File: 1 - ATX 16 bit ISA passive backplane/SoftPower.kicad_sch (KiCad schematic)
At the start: 41 parts, among them J19 ATX POWER, SW1 POWER, U1 74HCT14, U2 74HCT74, U3 LM7905

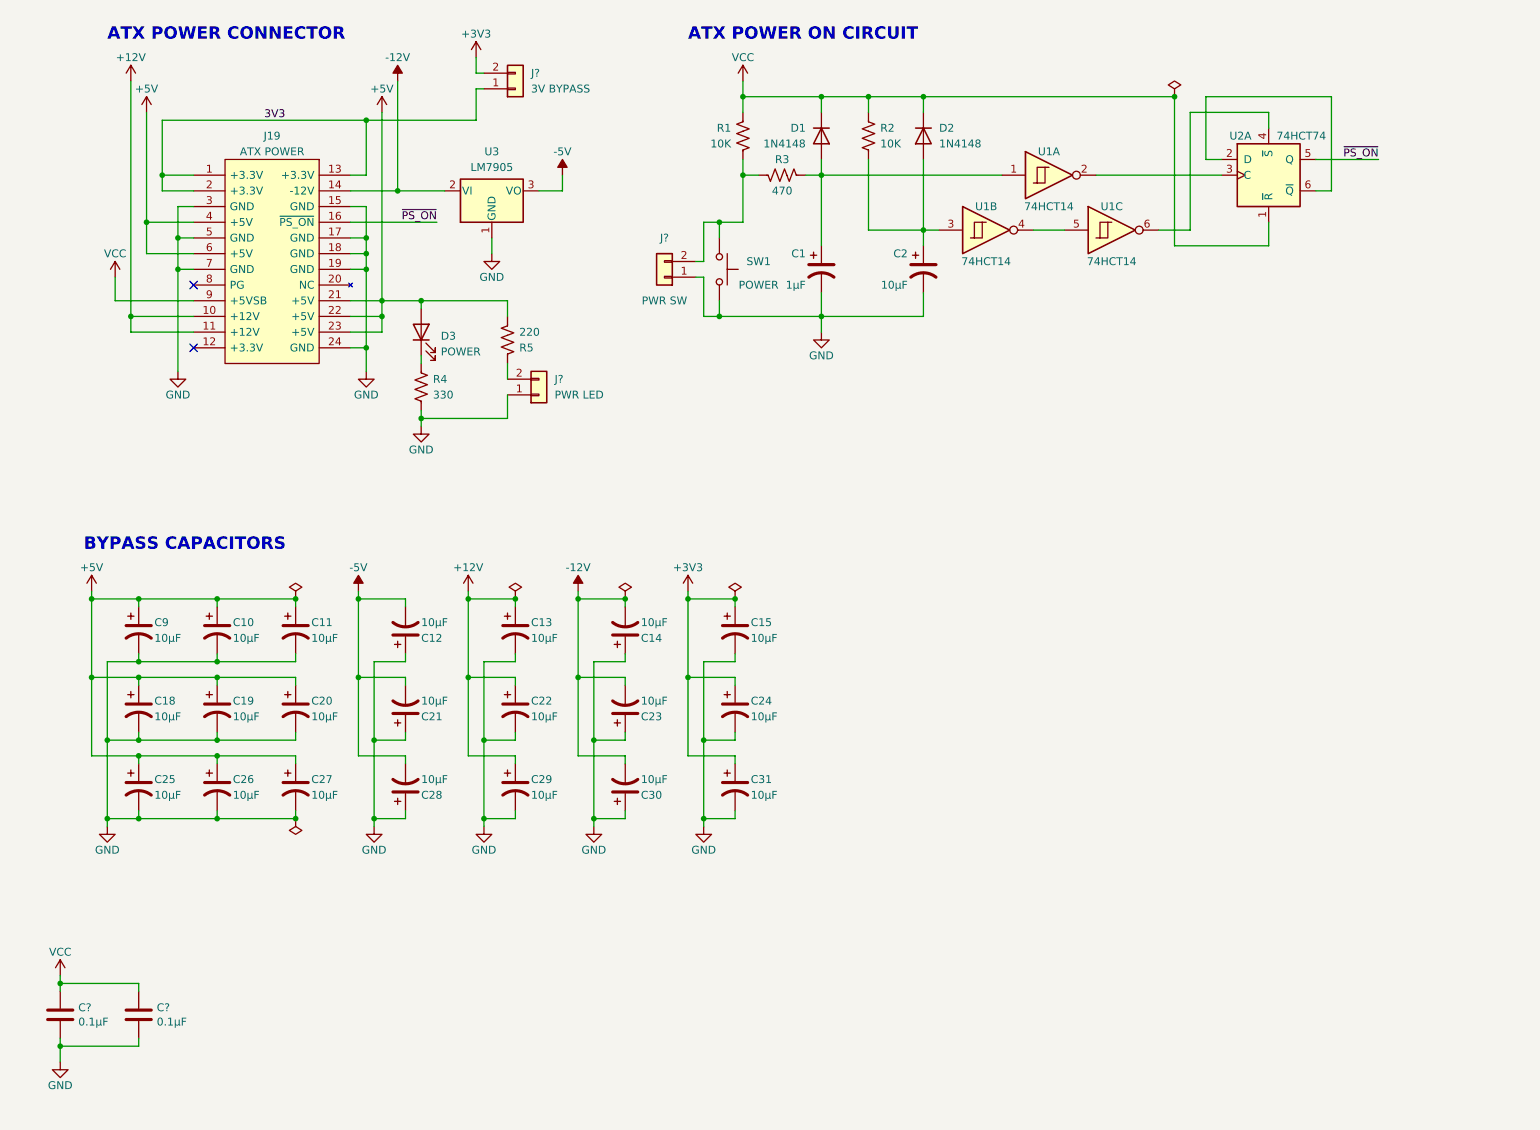
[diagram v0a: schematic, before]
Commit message: Removed unessential components and added capacitors on the bus lanes. Still need work for on the silkscreen side.
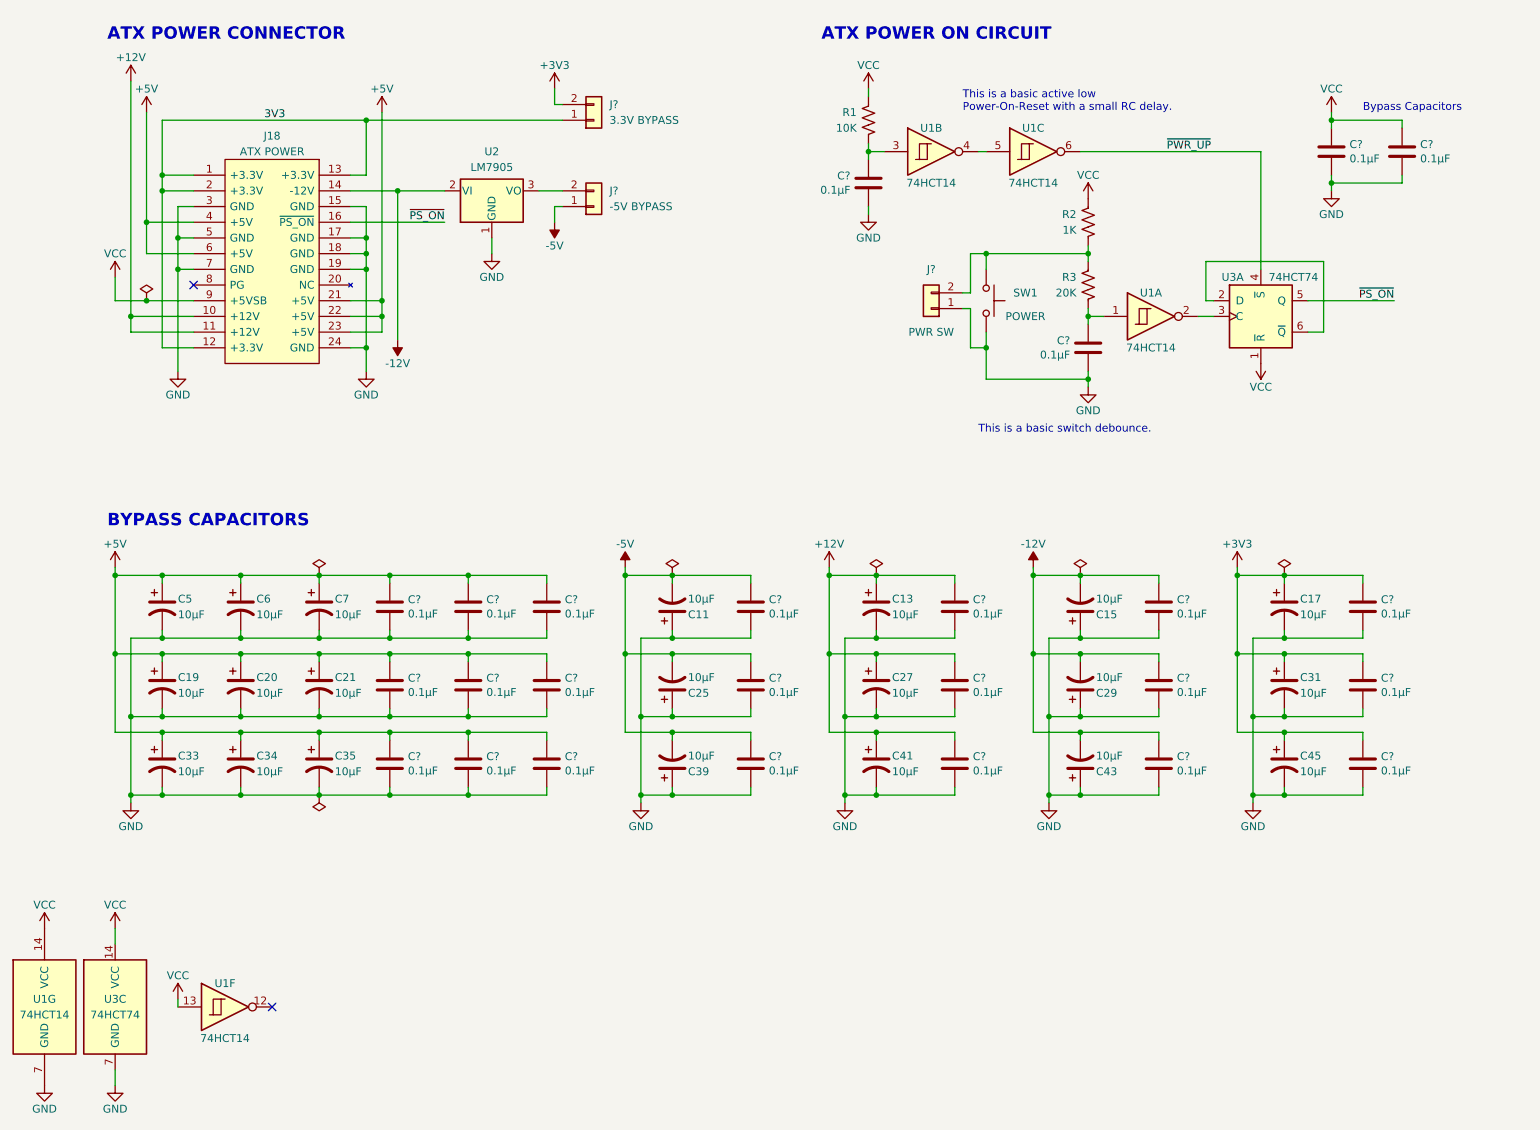
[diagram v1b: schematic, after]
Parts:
- removed C1: 1µF, Capacitor_THT:CP_Radial_D5.0mm_P2.50mm, symbol Device:C_Polarized_US
- removed C2: 10µF, Capacitor_THT:CP_Radial_D6.3mm_P2.50mm, symbol Device:C_Polarized_US
- removed C? (x2): 0.1µF, Capacitor_THT:C_Disc_D3.0mm_W1.6mm_P2.50mm, symbol Device:C
- removed D1, D2: 1N4148, Diode_THT:D_DO-35_SOD27_P7.62mm_Horizontal, symbol Diode:1N4148
- removed D3: POWER, LED_THT:LED_D3.0mm, symbol Device:LED
- removed J?: PWR LED, Connector_PinHeader_2.54mm:PinHeader_1x02_P2.54mm_Vertical, symbol Connector_Generic:Conn_01x02
- removed R4: 330, Resistor_THT:R_Axial_DIN0207_L6.3mm_D2.5mm_P10.16mm_Horizontal, symbol Device:R_US
- removed R5: 220, Resistor_THT:R_Axial_DIN0207_L6.3mm_D2.5mm_P10.16mm_Horizontal, symbol Device:R_US
- added C? (x25): 0.1µF, Capacitor_THT:C_Disc_D3.0mm_W1.6mm_P2.50mm, symbol Device:C
- added J?: -5V BYPASS, 0 - Library:PinHeader_1x2_Vertical (Modified), symbol Connector_Generic:Conn_01x02
- added unit 7 of U1
- added unit 6 of U1
- added unit 3 of U3
- J?: value 3V BYPASS -> 3.3V BYPASS
- J?: footprint Connector_PinHeader_2.54mm:PinHeader_1x02_P2.54mm_Vertical -> 0 - Library:PinHeader_1x2_Vertical (Modified)
- R2: value 10K -> 1K
- R3: value 470 -> 20K
- renumbered C12 to C11, C14 to C15, C15 to C17, C18 to C19, C19 to C20, C20 to C21, C21 to C25, C22 to C27, C23 to C29, C24 to C31, C25 to C33, C26 to C34, C27 to C35, C28 to C39, C29 to C41, C30 to C43, C31 to C45, C9 to C5, C10 to C6, C11 to C7, J19 to J18, U3 to U2, U2 to U3
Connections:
- net +12V: now also C?.1, C?.1, C?.1
- net +3V3: now also C?.1, C?.1, C?.1
- net +5V: now also C?.1, C?.1, C?.1, C?.1, C?.1, C?.1, C?.1, C?.1, C?.1
- net -12V: now also C?.1, C?.1, C?.1
- net -5V: now also C?.1, C?.1, C?.1, J?.1 (Pin_1); no longer U2.3 (VO)
- net 3V3: now also J18.12 (+3.3V)
- net GND: now also C?.2, C?.2, C?.2, C?.2, C?.2, C?.2, C?.2, C?.2, C?.2, C?.2, C?.2, C?.2, C?.2, C?.2, C?.2, C?.2, C?.2, C?.2, C?.2, C?.2, C?.2, C?.2, C?.2, C?.2, C?.2, U1.7 (GND), U3.7 (GND)
- net VCC: now also C?.1, C?.1, U1.13, U1.14 (VCC), U3.14 (VCC)
- net at R3.1: now also J?.2 (Pin_2), R2.2, SW1.2; no longer U1.1
- net ~{PWR_UP}: now reaches U1.6, U3.4 (~{S})
- net at U1.3: now also R1.2, C?.1; no longer R2.2
- new net: C?.1, R3.2, U1.1
- new net: J?.2 (Pin_2), U2.3 (VO)
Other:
- note added: "Bypass Capacitors"
- note added: "This is a basic active low Power-On-Reset with a small RC delay."
- note added: "This is a basic switch debounce."
- moved on the sheet: C11, C13, C15, C17, C19, C20, C21, C25, C27, C29, C31, C33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

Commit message: Minor tweaks to the backplane, and will be sending it out for manufacture
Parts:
- J18: footprint 0 - Library:ATX_PSU_CONN -> 0_Library:ATX_PSU_CONN
- J? (x2): footprint 0 - Library:PinHeader_1x2_Vertical (Modified) -> 0_Library:PinHeader_1x2_Vertical (Modified)
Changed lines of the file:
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@@
       (effects (font (size 1.27 1.27)) (justify left))
     )
-    (property "Footprint" "0 - Library:PinHeader_1x2_Vertical (Modified)" (at 110.49 54.61 0)
+    (property "Footprint" "0_Library:PinHeader_1x2_Vertical (Modified)" (at 110.49 54.61 0)
       (effects (font (size 1.27 1.27)) hide)
     )
@@
       (effects (font (size 1.27 1.27)))
     )
-    (property "Footprint" "0 - Library:ATX_PSU_CONN" (at 50.8 81.28 0)
+    (property "Footprint" "0_Library:ATX_PSU_CONN" (at 50.8 81.28 0)
       (effects (font (size 1.27 1.27)) (justify left) hide)
     )
@@
       (effects (font (size 1.27 1.27)))
     )
-    (property "Footprint" "0 - Library:PinHeader_1x2_Vertical (Modified)" (at 165.1 71.12 0)
-      (effects (font (size 1.27 1.27)) hide)
-    )
+    (property "Footprint" "0_Library:PinHeader_1x2_Vertical (Modified)" (at 165.1 71.12 0)
+      (effects (font (size 1.27 1.27)) hide)
+    )

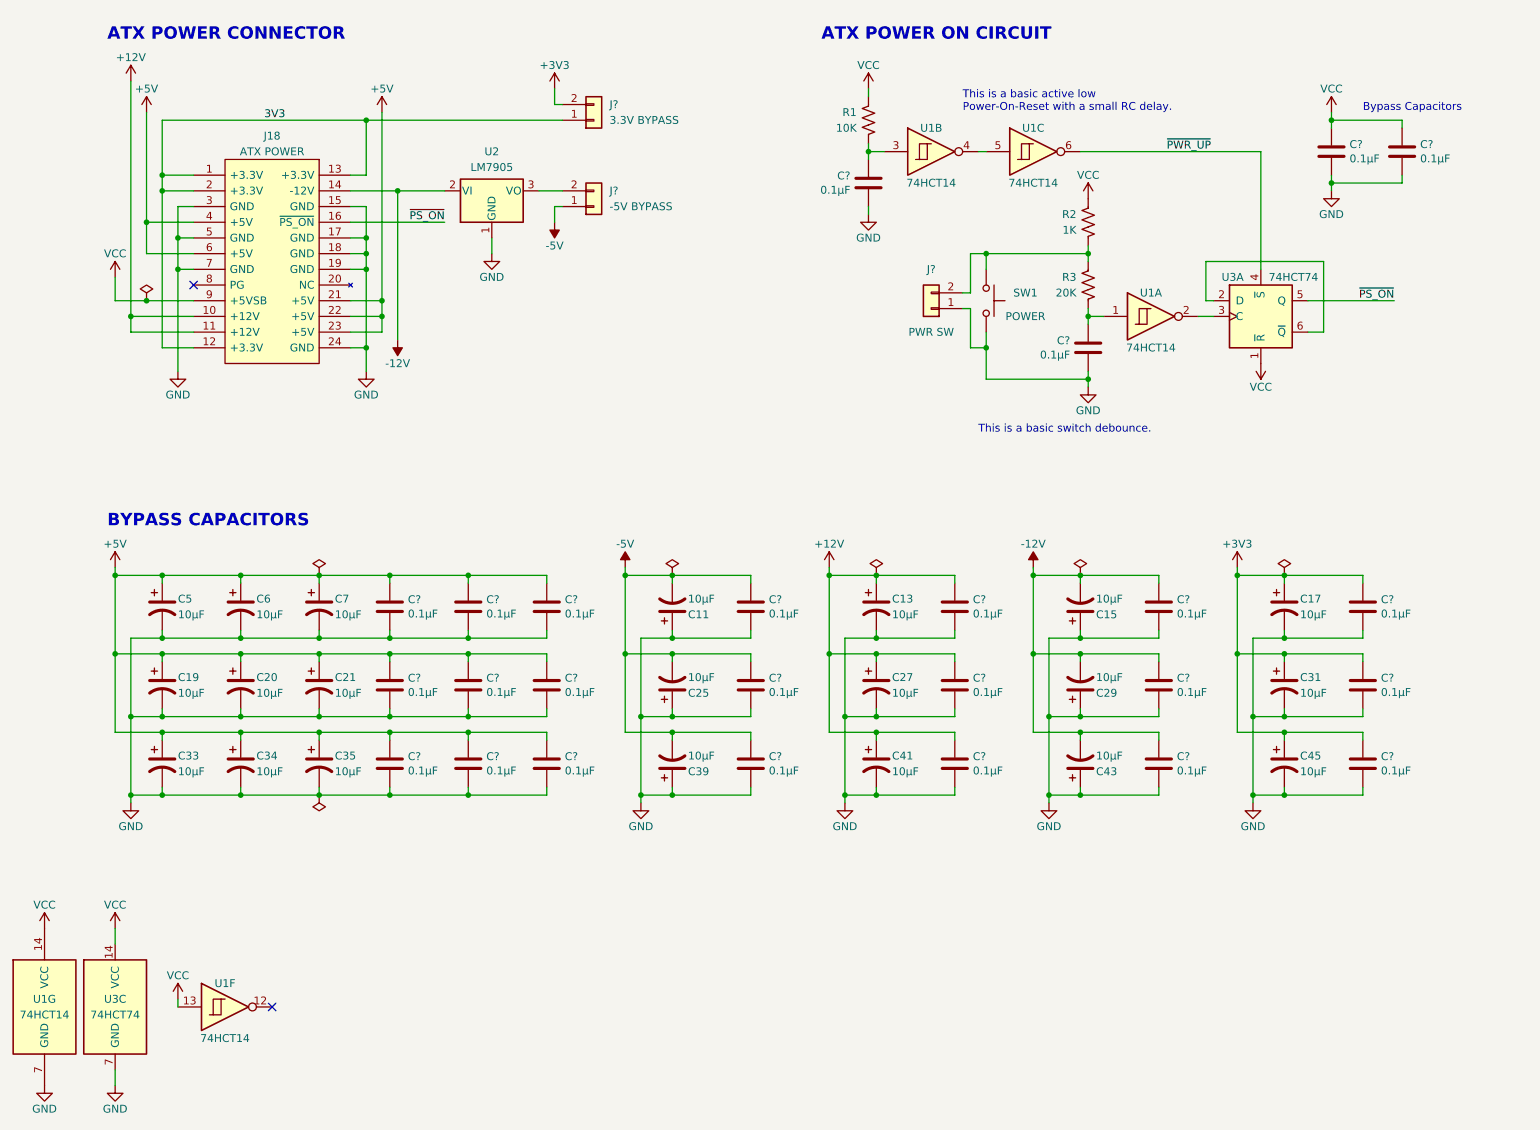
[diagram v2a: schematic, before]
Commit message: Updated disk activity circuit in mother board, and improved layout in CPU card
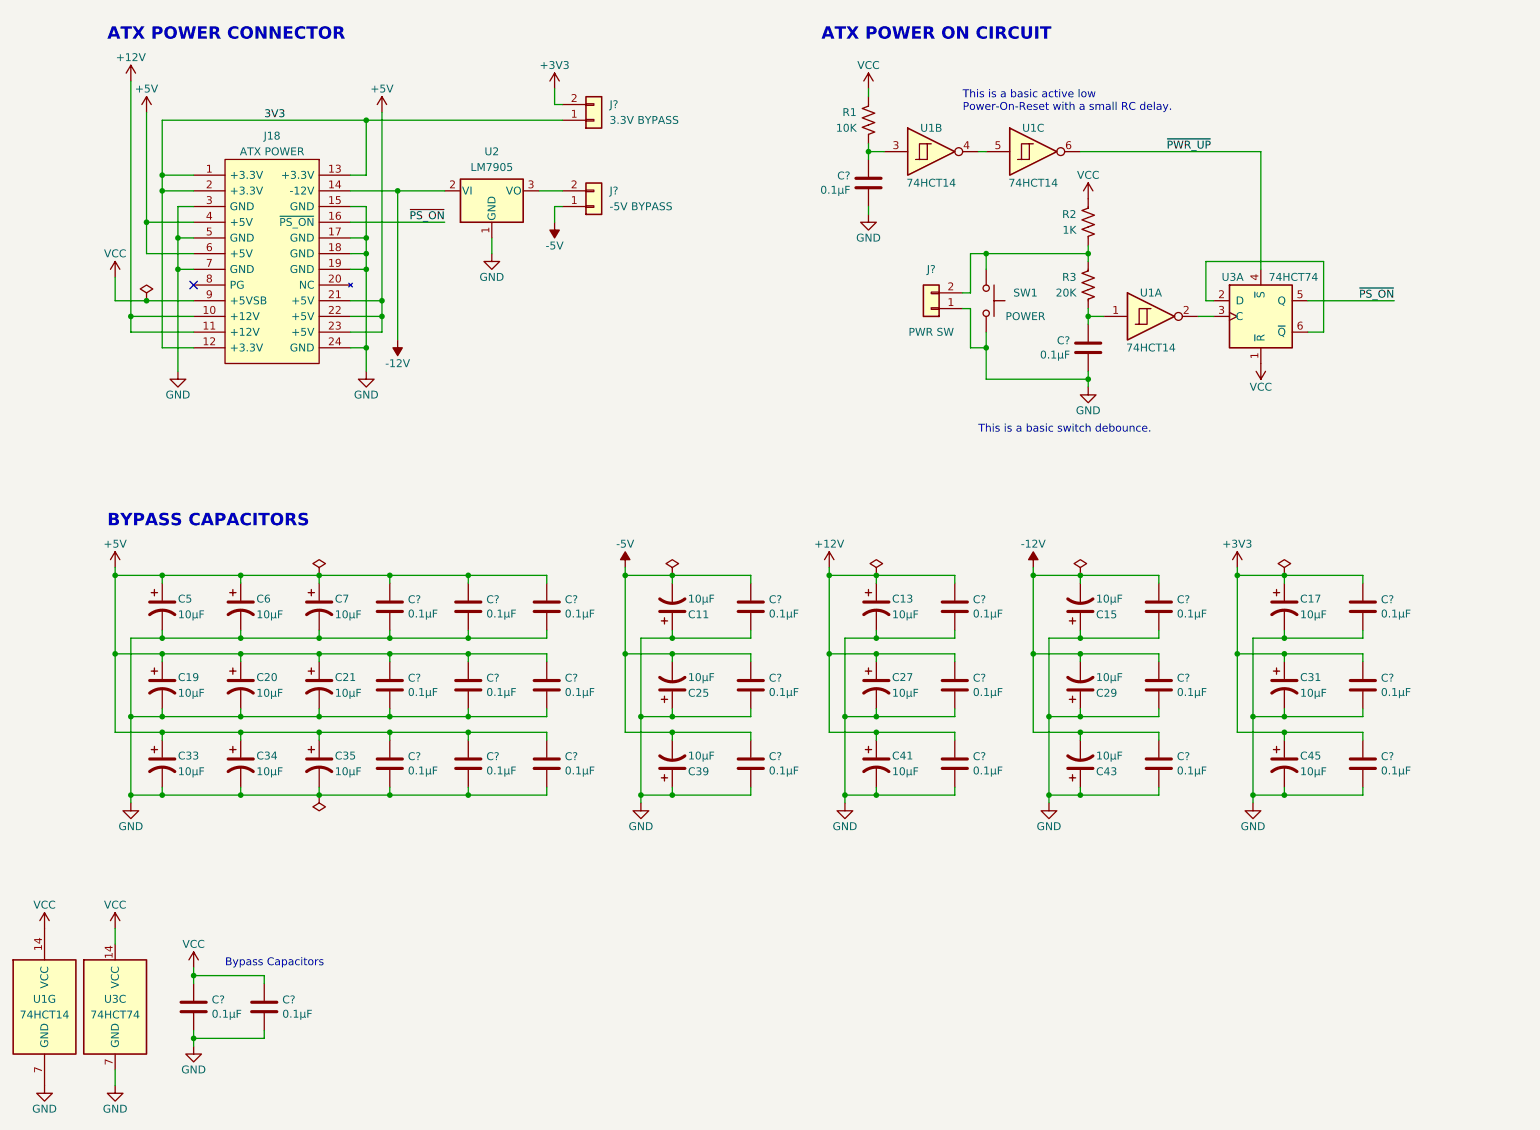
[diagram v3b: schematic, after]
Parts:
- removed C? (x2): 0.1µF, Capacitor_THT:C_Disc_D3.0mm_W1.6mm_P2.50mm, symbol Device:C
- removed unit 6 of U1
- added C? (x2): 0.1µF, Capacitor_THT:C_Disc_D3.0mm_W1.6mm_P2.50mm, symbol Device:C
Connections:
- net GND: now also C?.2, C?.2
- net VCC: now also C?.1, C?.1
- no-connect marks 2 -> 1
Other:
- title: (none) -> Power on circuit and BUS bypass capacitors

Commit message: Finally finalized the backplane to my liking.
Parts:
- removed C11, C25, C39: 10µF, Capacitor_THT:CP_Radial_D6.3mm_P2.50mm, symbol Device:C_Polarized_US
- removed C? (x5): 0.1µF, Capacitor_THT:C_Disc_D3.0mm_W1.6mm_P2.50mm, symbol Device:C
- removed J?: 3.3V BYPASS, Connector_PinHeader_2.54mm:PinHeader_1x02_P2.54mm_Vertical, symbol Connector_Generic:Conn_01x02
- removed J?: -5V BYPASS, 0_Library:PinHeader_1x2_Vertical (Modified), symbol Connector_Generic:Conn_01x02
- removed J?: PWR SW, 0_Library:PinHeader_1x2_Vertical (Modified), symbol Connector_Generic:Conn_01x02
- removed SW1: POWER, Button_Switch_THT:SW_PUSH-12mm, symbol Switch:SW_Push
- removed unit 7 of U1
- removed U2: LM7905, Package_TO_SOT_THT:TO-220-3_Horizontal_TabDown, symbol Regulator_Linear:LM7905_TO220
- removed unit 3 of U3
- added C?: 10µF, Capacitor_THT:CP_Radial_D6.3mm_P2.50mm, symbol Device:C_Polarized_US
- added C?: 22µF, Capacitor_THT:C_Disc_D3.0mm_W1.6mm_P2.50mm, symbol Device:C
- added C?: 1µF, Capacitor_THT:C_Disc_D3.0mm_W1.6mm_P2.50mm, symbol Device:C
- added J11: PWR IN SEL, Connector_PinHeader_2.54mm:PinHeader_2x03_P2.54mm_Vertical, symbol Connector_Generic:Conn_02x03_Odd_Even
- added J12: PWR SW SEL, Connector_PinHeader_2.54mm:PinHeader_2x03_P2.54mm_Vertical, symbol Connector_Generic:Conn_02x03_Odd_Even
- added J19: 3V/-5V, Connector_PinHeader_2.54mm:PinHeader_1x03_P2.54mm_Vertical, symbol Connector_Generic:Conn_01x03
- added J?: PWR_SW, 0_Library:PinHeader_1x2_Vertical (Modified), symbol Connector_Generic:Conn_01x02
- added J?: PWR_LED, 0_Library:PinHeader_1x2_Vertical (Modified), symbol Connector_Generic:Conn_01x02
- added J?: 5V DC (CP), Connector_BarrelJack:BarrelJack_Horizontal, symbol 0_Library:Barrel_Jack
- added Q? (x2): 2N3904, Package_TO_SOT_THT:TO-92_Inline_Wide, symbol Transistor_BJT:2N3904
- added Q?: IRF4905PBF, Package_TO_SOT_THT:TO-220-3_Horizontal_TabDown, symbol Transistor_FET:IRF4905
- added R? (x2): 220, Resistor_THT:R_Axial_DIN0207_L6.3mm_D2.5mm_P10.16mm_Horizontal, symbol Device:R_US
- added R?: 1K, Resistor_THT:R_Axial_DIN0207_L6.3mm_D2.5mm_P10.16mm_Horizontal, symbol Device:R_US
- added R? (x3): 100K, Resistor_THT:R_Axial_DIN0207_L6.3mm_D2.5mm_P10.16mm_Horizontal, symbol Device:R_US
- added SW?: POWER, 0_Library:Pushbutton_12mm_LED, symbol Switch:SW_Push_LED
- added U4: LM7905, Package_TO_SOT_THT:TO-220-3_Horizontal_TabDown, symbol Regulator_Linear:L7905
- added U?: LD1117V33, Package_TO_SOT_THT:TO-220-3_Horizontal_TabDown, symbol 0_Library:LM1117-3.3
- C? (x20): value 0.1µF -> 1µF
- renumbered C5 to C1, C34 to C10, C45 to C11, C7 to C13, C21 to C14, C35 to C15, C13 to C19, C19 to C2, C27 to C24, C41 to C29, C33 to C3, C15 to C31, C29 to C33, C43 to C35, C17 to C4, C31 to C6, C6 to C8, C20 to C9, J18 to J10, R1 to R4, R2 to R8, R3 to R9
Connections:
- net +3V3: now also J11.3 (Pin_3), J19.2 (Pin_2)
- net +5V: now also J11.4 (Pin_4), R?.2, R?.2; no longer J10.21 (+5V), J10.22 (+5V), J10.23 (+5V), J10.4 (+5V), J10.6 (+5V)
- net -12V: now also U4.2 (VI)
- net GND: now also C?.2, C?.2, C?.2, J12.6 (Pin_6), J?.2, J?.2 (Pin_2), J?.3, Q?.1 (E), R?.1, SW?.3 (K), U4.1 (GND), U?.1 (GND)
- net ATX: now reaches R8.2, R9.1
- net ATX: now also J12.5 (Pin_5)
- net 3V3 renamed ATX_3V3
- net ATX_3V3: now also J11.5 (Pin_5), J19.1 (Pin_1); no longer J10.12 (+3.3V)
- new net: J12.4 (Pin_4), J?.1 (Pin_1), SW?.1
- new net: J12.3 (Pin_3), J?.2 (Pin_2), SW?.2
- new net: Q?.1 (E), R?.2
- new net: Q?.1 (G), Q?.3 (C), R?.1
- new net: R?.1, SW?.4 (A)
- new net: J?.1 (Pin_1), R?.1
- new net ALT1: J12.1 (Pin_1), Q?.2 (B), Q?.2 (B), R?.1
- new net ALT2: C?.1, J12.2 (Pin_2), Q?.3 (C), R?.1
- new net ALT_3V3: C?.1, J11.1 (Pin_1), U?.2 (VO)
- new net ALT_5V: J11.2 (Pin_2), Q?.2 (D), R?.2, U?.3 (VI)
- new net ATX_-5V: J19.3 (Pin_3), U4.3 (VO)
- new net ATX_5V: J10.21 (+5V), J10.22 (+5V), J10.23 (+5V), J10.4 (+5V), J10.6 (+5V), J11.6 (Pin_6)
- new net Vin: C?.1, J?.1, Q?.3 (S), R?.2, R?.2
- no-connect marks 1 -> 2
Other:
- note added: "ALTERNATE POWER SOURCE WITH SOFT ON CIRCUIT"
- note added: "Select between -5V or 3V3 on lane B5"
- note removed: "Bypass Capacitors"
- moved on the sheet: C1, C10, C11, C13, C14, C15, C19, C2, C24, C29, C3, C31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
